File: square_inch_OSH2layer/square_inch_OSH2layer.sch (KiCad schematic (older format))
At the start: 2 parts

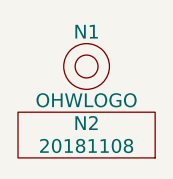
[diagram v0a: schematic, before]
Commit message: updated solderpaste expansion to 0%
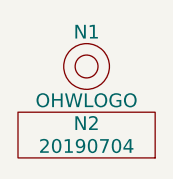
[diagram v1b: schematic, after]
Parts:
- N2: value 20181108 -> 20190704
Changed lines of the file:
@@
 EESchema Schematic File Version 4
-LIBS:OSH_Park_2_layer-cache
-EELAYER 26 0
+LIBS:square_inch_OSH2layer-cache
+EELAYER 29 0
 EELAYER END
 $Descr A4 11693 8268
@@
 P 850 7700
 F 0 "N2" H 850 7800 60  0000 C CNN
-F 1 "20181108" H 850 7700 60  0000 C CNN
+F 1 "20190704" H 850 7700 60  0000 C CNN
 F 2 "SquantorLabels:Label_version" H 850 7700 60  0001 C CNN
 F 3 "" H 850 7700 60  0001 C CNN
